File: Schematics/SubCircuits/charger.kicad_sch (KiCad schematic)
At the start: 15 parts, among them J1 USB-C, J2 Batt, U1 BQ25300

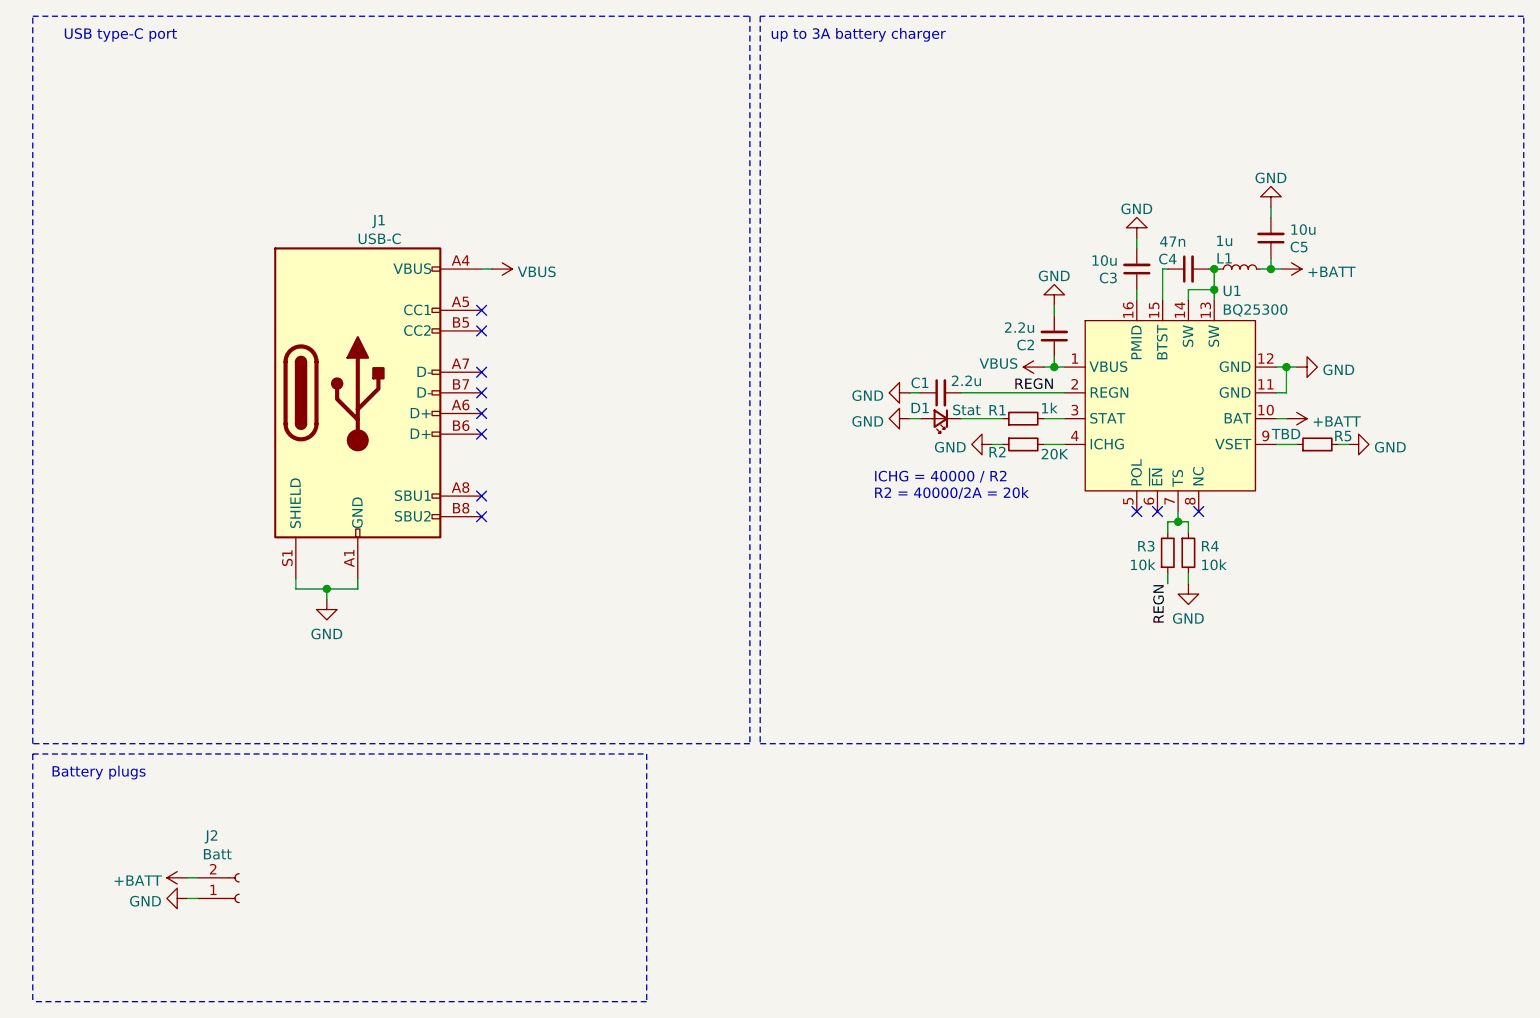
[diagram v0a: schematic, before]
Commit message: Added defunct subcircuit project
superseded by modular mainboard
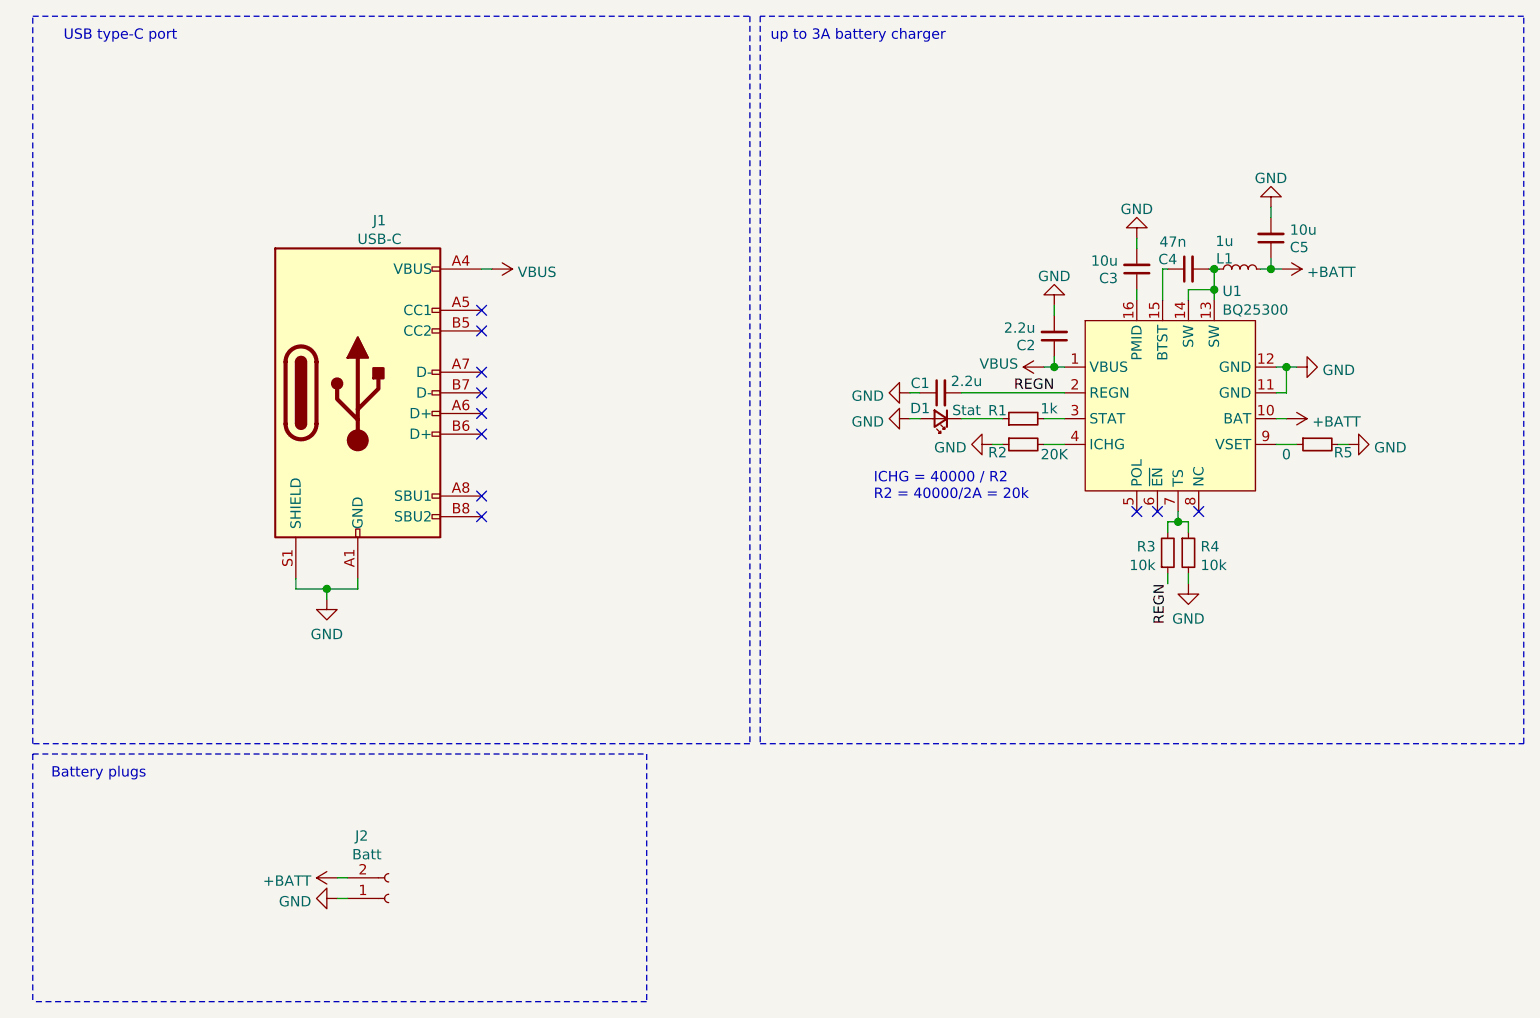
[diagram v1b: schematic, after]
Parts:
- D1: LCSC Part C268294 -> C268294
- J1: LCSC Part C165948 -> C165948
- R5: value TBD -> 0; LCSC Part (none) -> C15402
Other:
- moved on the sheet: J2
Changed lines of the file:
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@@
-(kicad_sch (version 20210126) (generator eeschema)
+(kicad_sch (version 20210406) (generator eeschema)
   (paper "A5")
   (title_block
@@
   (no_connect (at 151.765 74.295))
   (no_connect (at 156.845 74.295))
-  (wire (pts (xy 32.385 119.38) (xy 33.655 119.38))
-    (stroke (width 0) (type solid) (color 0 0 0 0))
-  )
-  (wire (pts (xy 32.385 121.92) (xy 33.655 121.92))
-    (stroke (width 0) (type solid) (color 0 0 0 0))
-  )
   (wire (pts (xy 45.72 82.55) (xy 45.72 83.82))
     (stroke (width 0) (type solid) (color 0 0 0 0))
@@
   )
   (wire (pts (xy 49.53 83.82) (xy 53.34 83.82))
+    (stroke (width 0) (type solid) (color 0 0 0 0))
+  )
+  (wire (pts (xy 50.8 119.38) (xy 52.07 119.38))
+    (stroke (width 0) (type solid) (color 0 0 0 0))
+  )
+  (wire (pts (xy 50.8 121.92) (xy 52.07 121.92))
     (stroke (width 0) (type solid) (color 0 0 0 0))
   )
@@
     (effects (font (size 1.27 1.27)) (justify right bottom))
   )
-  (symbol (lib_id "power:+BATT") (at 32.385 119.38 90) (unit 1)
-    (in_bom yes) (on_board yes)
-    (property "Reference" "#PWR0123" (id 0) (at 36.195 119.38 0)
-      (effects (font (size 1.27 1.27)) hide)
-    )
-    (property "Value" "+BATT" (id 1) (at 29.2099 119.7685 90)
-      (effects (font (size 1.27 1.27)) (justify left))
-    )
-    (property "Footprint" "" (id 2) (at 32.385 119.38 0)
-      (effects (font (size 1.27 1.27)) hide)
-    )
-    (property "Datasheet" "" (id 3) (at 32.385 119.38 0)
+  (symbol (lib_id "power:+BATT") (at 50.8 119.38 90) (unit 1)
+    (in_bom yes) (on_board yes)
+    (property "Reference" "#PWR0123" (id 0) (at 54.61 119.38 0)
+      (effects (font (size 1.27 1.27)) hide)
+    )
+    (property "Value" "+BATT" (id 1) (at 47.6249 119.7685 90)
+      (effects (font (size 1.27 1.27)) (justify left))
+    )
+    (property "Footprint" "" (id 2) (at 50.8 119.38 0)
+      (effects (font (size 1.27 1.27)) hide)
+    )
+    (property "Datasheet" "" (id 3) (at 50.8 119.38 0)
       (effects (font (size 1.27 1.27)) hide)
     )
@@
     (pin "2")
   )
-  (symbol (lib_id "power:GND") (at 32.385 121.92 270) (unit 1)
-    (in_bom yes) (on_board yes)
-    (property "Reference" "#PWR0103" (id 0) (at 26.035 121.92 0)
-      (effects (font (size 1.27 1.27)) hide)
-    )
-    (property "Value" "GND" (id 1) (at 29.21 122.3085 90)
-      (effects (font (size 1.27 1.27)) (justify right))
-    )
-    (property "Footprint" "" (id 2) (at 32.385 121.92 0)
-      (effects (font (size 1.27 1.27)) hide)
-    )
-    (property "Datasheet" "" (id 3) (at 32.385 121.92 0)
-      (effects (font (size 1.27 1.27)) hide)
-    )
-    (pin "1")
-  )
   (symbol (lib_id "power:GND") (at 49.53 85.09 0) (unit 1)
     (in_bom yes) (on_board yes)
@@
     )
     (property "Datasheet" "" (id 3) (at 49.53 85.09 0)
+      (effects (font (size 1.27 1.27)) hide)
+    )
+    (pin "1")
+  )
+  (symbol (lib_id "power:GND") (at 50.8 121.92 270) (unit 1)
+    (in_bom yes) (on_board yes)
+    (property "Reference" "#PWR0103" (id 0) (at 44.45 121.92 0)
+      (effects (font (size 1.27 1.27)) hide)
+    )
+    (property "Value" "GND" (id 1) (at 47.625 122.3085 90)
+      (effects (font (size 1.27 1.27)) (justify right))
+    )
+    (property "Footprint" "" (id 2) (at 50.8 121.92 0)
+      (effects (font (size 1.27 1.27)) hide)
+    )
+    (property "Datasheet" "" (id 3) (at 50.8 121.92 0)
       (effects (font (size 1.27 1.27)) hide)
     )
@@
     (pin "2")
   )
-  (symbol (lib_id "Device:R_Small") (at 171.45 66.04 90) (unit 1)
-    (in_bom yes) (on_board yes)
-    (property "Reference" "R5" (id 0) (at 174.625 65.0452 90))
-    (property "Value" "TBD" (id 1) (at 167.64 64.8039 90))
+  (symbol (lib_id "Device:R_Small") (at 171.45 66.04 90) (mirror x) (unit 1)
+    (in_bom yes) (on_board yes)
+    (property "Reference" "R5" (id 0) (at 174.625 67.0348 90))
+    (property "Value" "0" (id 1) (at 167.64 67.2761 90))
     (property "Footprint" "Resistor_SMD:R_0603_1608Metric" (id 2) (at 171.45 66.04 0)
       (effects (font (size 1.27 1.27)) hide)
     )
     (property "Datasheet" "~" (id 3) (at 171.45 66.04 0)
+      (effects (font (size 1.27 1.27)) hide)
+    )
+    (property "LCSC Part" "C15402" (id 4) (at 171.45 66.04 90)
       (effects (font (size 1.27 1.27)) hide)
     )
@@
       (effects (font (size 1.27 1.27)) hide)
     )
-    (property "LCSC Part" " C268294" (id 4) (at 125.095 62.865 0)
+    (property "LCSC Part" "C268294" (id 4) (at 125.095 62.865 0)
       (effects (font (size 1.27 1.27)) hide)
     )
@@
     (pin "2")
   )
-  (symbol (lib_id "Connector:Conn_01x02_Female") (at 38.735 121.92 0) (mirror x) (unit 1)
-    (in_bom yes) (on_board yes)
-    (property "Reference" "J2" (id 0) (at 35.4076 114.2196 0))
-    (property "Value" "Batt" (id 1) (at 36.0426 116.5183 0))
-    (property "Footprint" "Connector_JST:JST_PH_S2B-PH-K_1x02_P2.00mm_Horizontal" (id 2) (at 38.735 121.92 0)
-      (effects (font (size 1.27 1.27)) hide)
-    )
-    (property "Datasheet" "~" (id 3) (at 38.735 121.92 0)
-      (effects (font (size 1.27 1.27)) hide)
-    )
-    (property "LCSC Part" "C173752" (id 4) (at 38.735 121.92 0)
+  (symbol (lib_id "Connector:Conn_01x02_Female") (at 57.15 121.92 0) (mirror x) (unit 1)
+    (in_bom yes) (on_board yes)
+    (property "Reference" "J2" (id 0) (at 53.8226 114.2196 0))
+    (property "Value" "Batt" (id 1) (at 54.4576 116.5183 0))
+    (property "Footprint" "Connector_JST:JST_PH_S2B-PH-K_1x02_P2.00mm_Horizontal" (id 2) (at 57.15 121.92 0)
+      (effects (font (size 1.27 1.27)) hide)
+    )
+    (property "Datasheet" "~" (id 3) (at 57.15 121.92 0)
+      (effects (font (size 1.27 1.27)) hide)
+    )
+    (property "LCSC Part" "C173752" (id 4) (at 57.15 121.92 0)
       (effects (font (size 1.27 1.27)) hide)
     )
@@
       (effects (font (size 1.27 1.27)) hide)
     )
-    (property "LCSC Part" " C165948" (id 4) (at 53.34 59.69 0)
-      (effects (font (size 1.27 1.27)) hide)
-    )
+    (property "LCSC Part" "C165948" (id 4) (at 53.34 59.69 0)
+      (effects (font (size 1.27 1.27)) hide)
+    )
